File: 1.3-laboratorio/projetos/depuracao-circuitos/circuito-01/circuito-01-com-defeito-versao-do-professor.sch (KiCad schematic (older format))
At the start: 22 parts, among them J1 Conn_01x07_Male, J2 Conn_01x07_Male, J3 Conn_01x07_Male, J4 Conn_01x07_Male, J5 Conn_01x07_Male, J6 Conn_01x07_Male, J7 Conn_01x05, J8 Conn_01x05, P1 CONN_01X02, SW1 SW_DIP_x04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

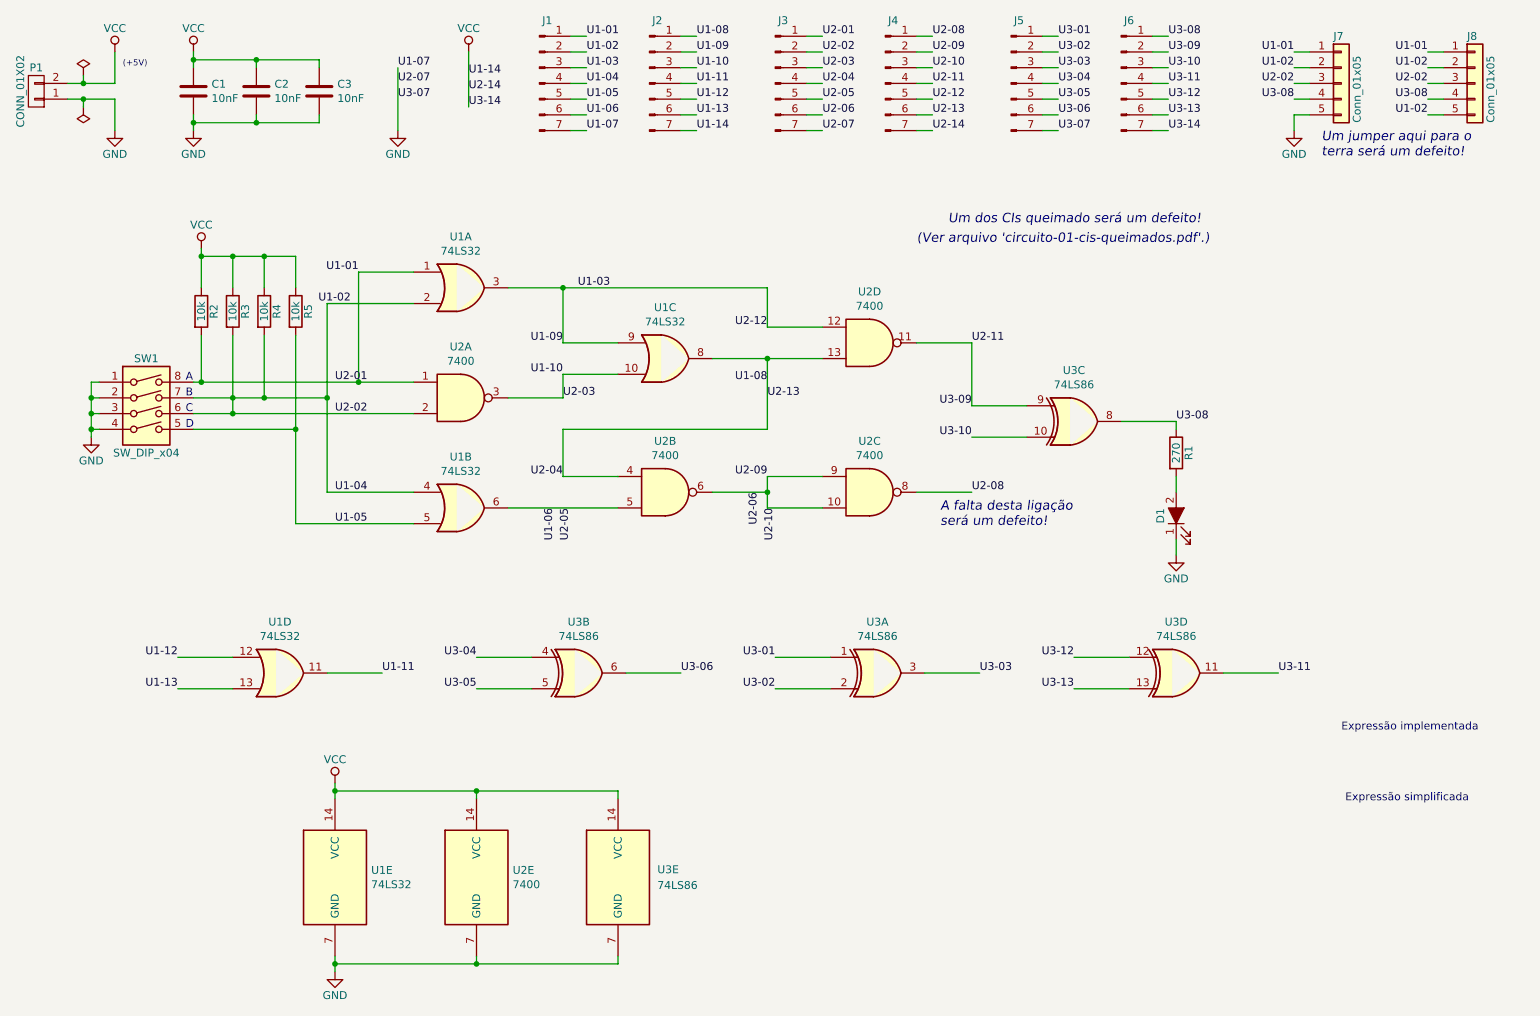
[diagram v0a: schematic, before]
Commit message: Revisão final das versões do esquema elétrico do Circuito para Depuração 01. Correções de identificação de variáveis de entrada realizadas, incluindo as correções nas expressões e Tabela-Verdade.
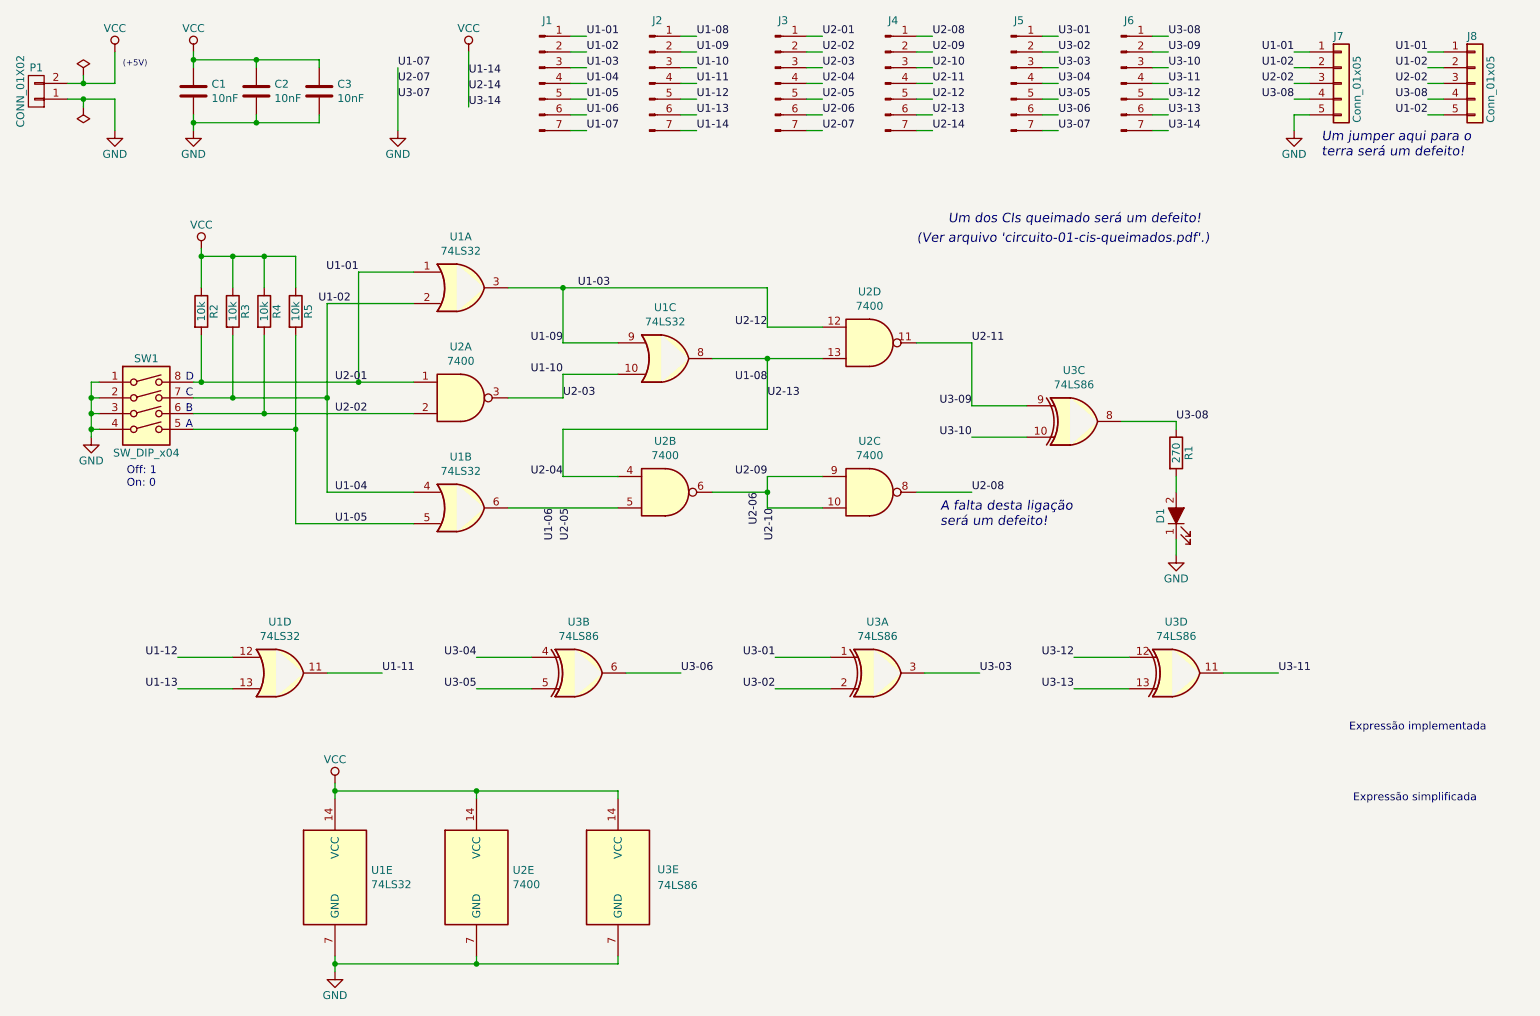
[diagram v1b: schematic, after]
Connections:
- net U1-02: no longer J3.2 (Pin_2), J7.3 (Pin_3), J8.3 (Pin_3), R4.2, SW1.6, U2.2
- new net U2-02: J3.2 (Pin_2), J7.3 (Pin_3), J8.3 (Pin_3), R4.2, SW1.6, U2.2
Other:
- note added: "Off: 1\nOn: 0"
